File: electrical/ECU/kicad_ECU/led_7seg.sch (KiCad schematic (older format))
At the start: 10 parts

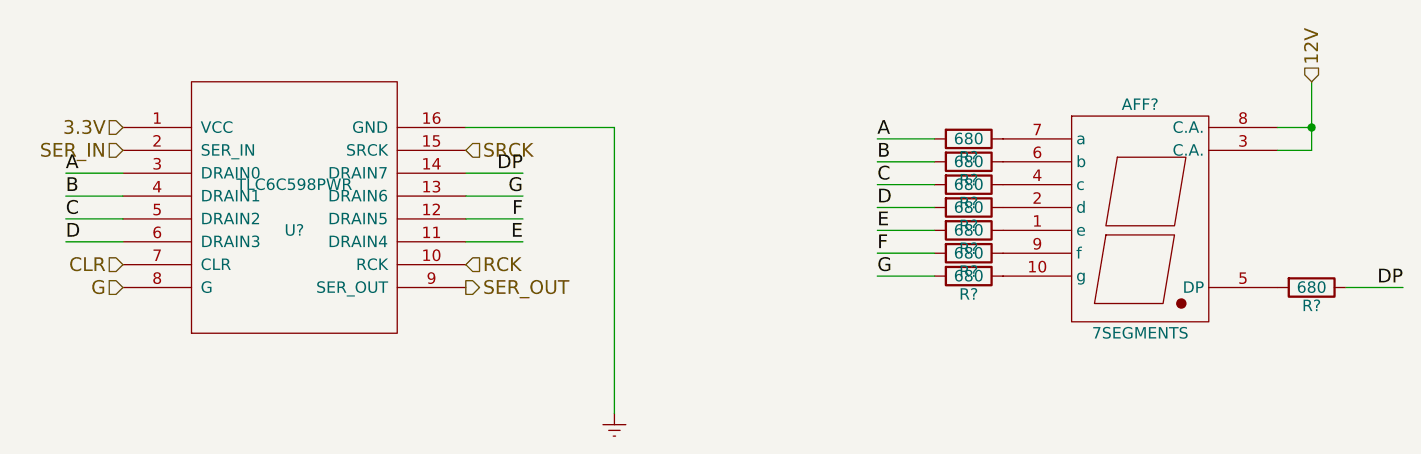
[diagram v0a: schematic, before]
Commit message: fixed some naming errors and initial round of double checking
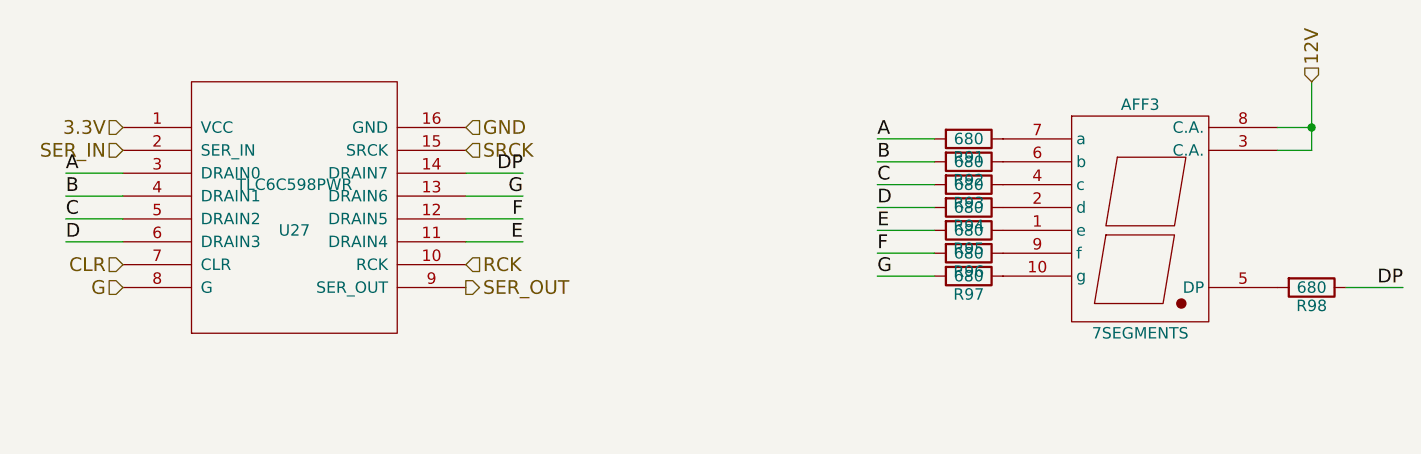
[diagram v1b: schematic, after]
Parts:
- gave numbers to parts that had none: 10
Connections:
- net Earth renamed GND
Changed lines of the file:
@@
 $Descr A4 11693 8268
 encoding utf-8
-Sheet 25 33
+Sheet 29 33
 Title ""
 Date ""
@@
 $EndDescr
 $Comp
-L 7SEGMENTS AFF?
+L 7SEGMENTS AFF1
 U 1 1 597A01F6
 P 7800 3550
-AR Path="/5978A36B/597907E6/597A01ED/597A01F6" Ref="AFF?"  Part="1"
-AR Path="/5978A36B/597907E6/597CC151/597A01F6" Ref="AFF?"  Part="1"
-AR Path="/5978A36B/597907E6/597CC684/597A01F6" Ref="AFF?"  Part="1"
-F 0 "AFF?" H 7800 4100 50  0000 C CNN
+AR Path="/5978A36B/597907E6/597A01ED/597A01F6" Ref="AFF1"  Part="1"
+AR Path="/5978A36B/597907E6/597CC151/597A01F6" Ref="AFF2"  Part="1"
+AR Path="/5978A36B/597907E6/597CC684/597A01F6" Ref="AFF3"  Part="1"
+F 0 "AFF3" H 7800 4100 50  0000 C CNN
 F 1 "7SEGMENTS" H 7800 3100 50  0000 C CNN
 F 2 "" H 7800 3550 50  0001 C CNN
@@
 $EndComp
 $Comp
-L TLC6C598PWR U?
+L TLC6C598PWR U25
 U 1 1 597A021D
 P 4100 3450
-AR Path="/5978A36B/597907E6/597A01ED/597A021D" Ref="U?"  Part="1"
-AR Path="/5978A36B/597907E6/597CC151/597A021D" Ref="U?"  Part="1"
-AR Path="/5978A36B/597907E6/597CC684/597A021D" Ref="U?"  Part="1"
-F 0 "U?" H 4100 3350 50  0000 C CNN
+AR Path="/5978A36B/597907E6/597A01ED/597A021D" Ref="U25"  Part="1"
+AR Path="/5978A36B/597907E6/597CC151/597A021D" Ref="U26"  Part="1"
+AR Path="/5978A36B/597907E6/597CC684/597A021D" Ref="U27"  Part="1"
+F 0 "U27" H 4100 3350 50  0000 C CNN
 F 1 "TLC6C598PWR" H 4100 3550 50  0000 C CNN
 F 2 "MODULE" H 4100 3450 50  0001 C CNN
@@
 SER_OUT
 $Comp
-L R R?
+L R R75
 U 1 1 597A0AE9
 P 7050 3150
-AR Path="/5978A36B/597907E6/597A01ED/597A0AE9" Ref="R?"  Part="1"
-AR Path="/5978A36B/597907E6/597CC151/597A0AE9" Ref="R?"  Part="1"
-AR Path="/5978A36B/597907E6/597CC684/597A0AE9" Ref="R?"  Part="1"
-F 0 "R?" V 7130 3150 50  0000 C CNN
+AR Path="/5978A36B/597907E6/597A01ED/597A0AE9" Ref="R75"  Part="1"
+AR Path="/5978A36B/597907E6/597CC151/597A0AE9" Ref="R83"  Part="1"
+AR Path="/5978A36B/597907E6/597CC684/597A0AE9" Ref="R91"  Part="1"
+F 0 "R91" V 7130 3150 50  0000 C CNN
 F 1 "680" V 7050 3150 50  0000 C CNN
 F 2 "" V 6980 3150 50  0001 C CNN
@@
 $EndComp
 $Comp
-L R R?
+L R R76
 U 1 1 597A0B81
 P 7050 3250
-AR Path="/5978A36B/597907E6/597A01ED/597A0B81" Ref="R?"  Part="1"
-AR Path="/5978A36B/597907E6/597CC151/597A0B81" Ref="R?"  Part="1"
-AR Path="/5978A36B/597907E6/597CC684/597A0B81" Ref="R?"  Part="1"
-F 0 "R?" V 7130 3250 50  0000 C CNN
+AR Path="/5978A36B/597907E6/597A01ED/597A0B81" Ref="R76"  Part="1"
+AR Path="/5978A36B/597907E6/597CC151/597A0B81" Ref="R84"  Part="1"
+AR Path="/5978A36B/597907E6/597CC684/597A0B81" Ref="R92"  Part="1"
+F 0 "R92" V 7130 3250 50  0000 C CNN
 F 1 "680" V 7050 3250 50  0000 C CNN
 F 2 "" V 6980 3250 50  0001 C CNN
@@
 $EndComp
 $Comp
-L R R?
+L R R77
 U 1 1 597A0BBD
 P 7050 3350
-AR Path="/5978A36B/597907E6/597A01ED/597A0BBD" Ref="R?"  Part="1"
-AR Path="/5978A36B/597907E6/597CC151/597A0BBD" Ref="R?"  Part="1"
-AR Path="/5978A36B/597907E6/597CC684/597A0BBD" Ref="R?"  Part="1"
-F 0 "R?" V 7130 3350 50  0000 C CNN
+AR Path="/5978A36B/597907E6/597A01ED/597A0BBD" Ref="R77"  Part="1"
+AR Path="/5978A36B/597907E6/597CC151/597A0BBD" Ref="R85"  Part="1"
+AR Path="/5978A36B/597907E6/597CC684/597A0BBD" Ref="R93"  Part="1"
+F 0 "R93" V 7130 3350 50  0000 C CNN
 F 1 "680" V 7050 3350 50  0000 C CNN
 F 2 "" V 6980 3350 50  0001 C CNN
@@
 $EndComp
 $Comp
-L R R?
+L R R78
 U 1 1 597A0BC3
 P 7050 3450
-AR Path="/5978A36B/597907E6/597A01ED/597A0BC3" Ref="R?"  Part="1"
-AR Path="/5978A36B/597907E6/597CC151/597A0BC3" Ref="R?"  Part="1"
-AR Path="/5978A36B/597907E6/597CC684/597A0BC3" Ref="R?"  Part="1"
-F 0 "R?" V 7130 3450 50  0000 C CNN
+AR Path="/5978A36B/597907E6/597A01ED/597A0BC3" Ref="R78"  Part="1"
+AR Path="/5978A36B/597907E6/597CC151/597A0BC3" Ref="R86"  Part="1"
+AR Path="/5978A36B/597907E6/597CC684/597A0BC3" Ref="R94"  Part="1"
+F 0 "R94" V 7130 3450 50  0000 C CNN
 F 1 "680" V 7050 3450 50  0000 C CNN
 F 2 "" V 6980 3450 50  0001 C CNN
@@
 $EndComp
 $Comp
-L R R?
+L R R79
 U 1 1 597A0C0D
 P 7050 3550
-AR Path="/5978A36B/597907E6/597A01ED/597A0C0D" Ref="R?"  Part="1"
-AR Path="/5978A36B/597907E6/597CC151/597A0C0D" Ref="R?"  Part="1"
-AR Path="/5978A36B/597907E6/597CC684/597A0C0D" Ref="R?"  Part="1"
-F 0 "R?" V 7130 3550 50  0000 C CNN
+AR Path="/5978A36B/597907E6/597A01ED/597A0C0D" Ref="R79"  Part="1"
+AR Path="/5978A36B/597907E6/597CC151/597A0C0D" Ref="R87"  Part="1"
+AR Path="/5978A36B/597907E6/597CC684/597A0C0D" Ref="R95"  Part="1"
+F 0 "R95" V 7130 3550 50  0000 C CNN
 F 1 "680" V 7050 3550 50  0000 C CNN
 F 2 "" V 6980 3550 50  0001 C CNN
@@
 $EndComp
 $Comp
-L R R?
+L R R80
 U 1 1 597A0C13
 P 7050 3650
-AR Path="/5978A36B/597907E6/597A01ED/597A0C13" Ref="R?"  Part="1"
-AR Path="/5978A36B/597907E6/597CC151/597A0C13" Ref="R?"  Part="1"
-AR Path="/5978A36B/597907E6/597CC684/597A0C13" Ref="R?"  Part="1"
-F 0 "R?" V 7130 3650 50  0000 C CNN
+AR Path="/5978A36B/597907E6/597A01ED/597A0C13" Ref="R80"  Part="1"
+AR Path="/5978A36B/597907E6/597CC151/597A0C13" Ref="R88"  Part="1"
+AR Path="/5978A36B/597907E6/597CC684/597A0C13" Ref="R96"  Part="1"
+F 0 "R96" V 7130 3650 50  0000 C CNN
 F 1 "680" V 7050 3650 50  0000 C CNN
 F 2 "" V 6980 3650 50  0001 C CNN
@@
 $EndComp
 $Comp
-L R R?
+L R R81
 U 1 1 597A0C19
 P 7050 3750
-AR Path="/5978A36B/597907E6/597A01ED/597A0C19" Ref="R?"  Part="1"
-AR Path="/5978A36B/597907E6/597CC151/597A0C19" Ref="R?"  Part="1"
-AR Path="/5978A36B/597907E6/597CC684/597A0C19" Ref="R?"  Part="1"
-F 0 "R?" V 7130 3750 50  0000 C CNN
+AR Path="/5978A36B/597907E6/597A01ED/597A0C19" Ref="R81"  Part="1"
+AR Path="/5978A36B/597907E6/597CC151/597A0C19" Ref="R89"  Part="1"
+AR Path="/5978A36B/597907E6/597CC684/597A0C19" Ref="R97"  Part="1"
+F 0 "R97" V 7130 3750 50  0000 C CNN
 F 1 "680" V 7050 3750 50  0000 C CNN
 F 2 "" V 6980 3750 50  0001 C CNN
@@
 $EndComp
 $Comp
-L R R?
+L R R82
 U 1 1 597A0C64
 P 8550 3800
-AR Path="/5978A36B/597907E6/597A01ED/597A0C64" Ref="R?"  Part="1"
-AR Path="/5978A36B/597907E6/597CC151/597A0C64" Ref="R?"  Part="1"
-AR Path="/5978A36B/597907E6/597CC684/597A0C64" Ref="R?"  Part="1"
-F 0 "R?" V 8630 3800 50  0000 C CNN
+AR Path="/5978A36B/597907E6/597A01ED/597A0C64" Ref="R82"  Part="1"
+AR Path="/5978A36B/597907E6/597CC151/597A0C64" Ref="R90"  Part="1"
+AR Path="/5978A36B/597907E6/597CC684/597A0C64" Ref="R98"  Part="1"
+F 0 "R98" V 8630 3800 50  0000 C CNN
 F 1 "680" V 8550 3800 50  0000 C CNN
 F 2 "" V 8480 3800 50  0001 C CNN
@@
 Text Label 5100 3300 2    60   ~ 0
 DP
-$Comp
-L Earth #PWR?
-U 1 1 597A0EF5
-P 5500 4350
-AR Path="/5978A36B/597907E6/597A01ED/597A0EF5" Ref="#PWR?"  Part="1"
-AR Path="/5978A36B/597907E6/597CC151/597A0EF5" Ref="#PWR?"  Part="1"
-AR Path="/5978A36B/597907E6/597CC684/597A0EF5" Ref="#PWR?"  Part="1"
-F 0 "#PWR?" H 5500 4100 50  0001 C CNN
-F 1 "Earth" H 5500 4200 50  0001 C CNN
-F 2 "" H 5500 4350 50  0001 C CNN
-F 3 "" H 5500 4350 50  0001 C CNN
-	1    5500 4350
-	1    0    0    -1
-$EndComp
-Wire Wire Line
-	4850 3100 5500 3100
-Wire Wire Line
-	5500 3100 5500 4350
+Text HLabel 4850 3100 2    60   Input ~ 0
+GND
 $EndSCHEMATC

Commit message: minor naming change
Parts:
- renumbered AFF1 to AFF2701, R75 to R2701, R76 to R2702, R77 to R2703, R78 to R2704, R79 to R2705, R80 to R2706, R81 to R2707, R82 to R2708, U25 to U2701
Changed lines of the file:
@@
 $EndDescr
 $Comp
-L 7SEGMENTS AFF1
+L 7SEGMENTS AFF2701
 U 1 1 597A01F6
 P 7800 3550
-AR Path="/5978A36B/597907E6/597A01ED/597A01F6" Ref="AFF1"  Part="1"
-AR Path="/5978A36B/597907E6/597CC151/597A01F6" Ref="AFF2"  Part="1"
-AR Path="/5978A36B/597907E6/597CC684/597A01F6" Ref="AFF3"  Part="1"
-F 0 "AFF3" H 7800 4100 50  0000 C CNN
+AR Path="/5978A36B/597907E6/597A01ED/597A01F6" Ref="AFF2701"  Part="1"
+AR Path="/5978A36B/597907E6/597CC151/597A01F6" Ref="AFF2801"  Part="1"
+AR Path="/5978A36B/597907E6/597CC684/597A01F6" Ref="AFF2901"  Part="1"
+F 0 "AFF2901" H 7800 4100 50  0000 C CNN
 F 1 "7SEGMENTS" H 7800 3100 50  0000 C CNN
 F 2 "" H 7800 3550 50  0001 C CNN
@@
 $EndComp
 $Comp
-L TLC6C598PWR U25
+L TLC6C598PWR U2701
 U 1 1 597A021D
 P 4100 3450
-AR Path="/5978A36B/597907E6/597A01ED/597A021D" Ref="U25"  Part="1"
-AR Path="/5978A36B/597907E6/597CC151/597A021D" Ref="U26"  Part="1"
-AR Path="/5978A36B/597907E6/597CC684/597A021D" Ref="U27"  Part="1"
-F 0 "U27" H 4100 3350 50  0000 C CNN
+AR Path="/5978A36B/597907E6/597A01ED/597A021D" Ref="U2701"  Part="1"
+AR Path="/5978A36B/597907E6/597CC151/597A021D" Ref="U2801"  Part="1"
+AR Path="/5978A36B/597907E6/597CC684/597A021D" Ref="U2901"  Part="1"
+F 0 "U2901" H 4100 3350 50  0000 C CNN
 F 1 "TLC6C598PWR" H 4100 3550 50  0000 C CNN
 F 2 "MODULE" H 4100 3450 50  0001 C CNN
@@
 SER_OUT
 $Comp
-L R R75
+L R R2701
 U 1 1 597A0AE9
 P 7050 3150
-AR Path="/5978A36B/597907E6/597A01ED/597A0AE9" Ref="R75"  Part="1"
-AR Path="/5978A36B/597907E6/597CC151/597A0AE9" Ref="R83"  Part="1"
-AR Path="/5978A36B/597907E6/597CC684/597A0AE9" Ref="R91"  Part="1"
-F 0 "R91" V 7130 3150 50  0000 C CNN
+AR Path="/5978A36B/597907E6/597A01ED/597A0AE9" Ref="R2701"  Part="1"
+AR Path="/5978A36B/597907E6/597CC151/597A0AE9" Ref="R2801"  Part="1"
+AR Path="/5978A36B/597907E6/597CC684/597A0AE9" Ref="R2901"  Part="1"
+F 0 "R2901" V 7130 3150 50  0000 C CNN
 F 1 "680" V 7050 3150 50  0000 C CNN
 F 2 "" V 6980 3150 50  0001 C CNN
@@
 $EndComp
 $Comp
-L R R76
+L R R2702
 U 1 1 597A0B81
 P 7050 3250
-AR Path="/5978A36B/597907E6/597A01ED/597A0B81" Ref="R76"  Part="1"
-AR Path="/5978A36B/597907E6/597CC151/597A0B81" Ref="R84"  Part="1"
-AR Path="/5978A36B/597907E6/597CC684/597A0B81" Ref="R92"  Part="1"
-F 0 "R92" V 7130 3250 50  0000 C CNN
+AR Path="/5978A36B/597907E6/597A01ED/597A0B81" Ref="R2702"  Part="1"
+AR Path="/5978A36B/597907E6/597CC151/597A0B81" Ref="R2802"  Part="1"
+AR Path="/5978A36B/597907E6/597CC684/597A0B81" Ref="R2902"  Part="1"
+F 0 "R2902" V 7130 3250 50  0000 C CNN
 F 1 "680" V 7050 3250 50  0000 C CNN
 F 2 "" V 6980 3250 50  0001 C CNN
@@
 $EndComp
 $Comp
-L R R77
+L R R2703
 U 1 1 597A0BBD
 P 7050 3350
-AR Path="/5978A36B/597907E6/597A01ED/597A0BBD" Ref="R77"  Part="1"
-AR Path="/5978A36B/597907E6/597CC151/597A0BBD" Ref="R85"  Part="1"
-AR Path="/5978A36B/597907E6/597CC684/597A0BBD" Ref="R93"  Part="1"
-F 0 "R93" V 7130 3350 50  0000 C CNN
+AR Path="/5978A36B/597907E6/597A01ED/597A0BBD" Ref="R2703"  Part="1"
+AR Path="/5978A36B/597907E6/597CC151/597A0BBD" Ref="R2803"  Part="1"
+AR Path="/5978A36B/597907E6/597CC684/597A0BBD" Ref="R2903"  Part="1"
+F 0 "R2903" V 7130 3350 50  0000 C CNN
 F 1 "680" V 7050 3350 50  0000 C CNN
 F 2 "" V 6980 3350 50  0001 C CNN
@@
 $EndComp
 $Comp
-L R R78
+L R R2704
 U 1 1 597A0BC3
 P 7050 3450
-AR Path="/5978A36B/597907E6/597A01ED/597A0BC3" Ref="R78"  Part="1"
-AR Path="/5978A36B/597907E6/597CC151/597A0BC3" Ref="R86"  Part="1"
-AR Path="/5978A36B/597907E6/597CC684/597A0BC3" Ref="R94"  Part="1"
-F 0 "R94" V 7130 3450 50  0000 C CNN
+AR Path="/5978A36B/597907E6/597A01ED/597A0BC3" Ref="R2704"  Part="1"
+AR Path="/5978A36B/597907E6/597CC151/597A0BC3" Ref="R2804"  Part="1"
+AR Path="/5978A36B/597907E6/597CC684/597A0BC3" Ref="R2904"  Part="1"
+F 0 "R2904" V 7130 3450 50  0000 C CNN
 F 1 "680" V 7050 3450 50  0000 C CNN
 F 2 "" V 6980 3450 50  0001 C CNN
@@
 $EndComp
 $Comp
-L R R79
+L R R2705
 U 1 1 597A0C0D
 P 7050 3550
-AR Path="/5978A36B/597907E6/597A01ED/597A0C0D" Ref="R79"  Part="1"
-AR Path="/5978A36B/597907E6/597CC151/597A0C0D" Ref="R87"  Part="1"
-AR Path="/5978A36B/597907E6/597CC684/597A0C0D" Ref="R95"  Part="1"
-F 0 "R95" V 7130 3550 50  0000 C CNN
+AR Path="/5978A36B/597907E6/597A01ED/597A0C0D" Ref="R2705"  Part="1"
+AR Path="/5978A36B/597907E6/597CC151/597A0C0D" Ref="R2805"  Part="1"
+AR Path="/5978A36B/597907E6/597CC684/597A0C0D" Ref="R2905"  Part="1"
+F 0 "R2905" V 7130 3550 50  0000 C CNN
 F 1 "680" V 7050 3550 50  0000 C CNN
 F 2 "" V 6980 3550 50  0001 C CNN
@@
 $EndComp
 $Comp
-L R R80
+L R R2706
 U 1 1 597A0C13
 P 7050 3650
-AR Path="/5978A36B/597907E6/597A01ED/597A0C13" Ref="R80"  Part="1"
-AR Path="/5978A36B/597907E6/597CC151/597A0C13" Ref="R88"  Part="1"
-AR Path="/5978A36B/597907E6/597CC684/597A0C13" Ref="R96"  Part="1"
-F 0 "R96" V 7130 3650 50  0000 C CNN
+AR Path="/5978A36B/597907E6/597A01ED/597A0C13" Ref="R2706"  Part="1"
+AR Path="/5978A36B/597907E6/597CC151/597A0C13" Ref="R2806"  Part="1"
+AR Path="/5978A36B/597907E6/597CC684/597A0C13" Ref="R2906"  Part="1"
+F 0 "R2906" V 7130 3650 50  0000 C CNN
 F 1 "680" V 7050 3650 50  0000 C CNN
 F 2 "" V 6980 3650 50  0001 C CNN
@@
 $EndComp
 $Comp
-L R R81
+L R R2707
 U 1 1 597A0C19
 P 7050 3750
-AR Path="/5978A36B/597907E6/597A01ED/597A0C19" Ref="R81"  Part="1"
-AR Path="/5978A36B/597907E6/597CC151/597A0C19" Ref="R89"  Part="1"
-AR Path="/5978A36B/597907E6/597CC684/597A0C19" Ref="R97"  Part="1"
-F 0 "R97" V 7130 3750 50  0000 C CNN
+AR Path="/5978A36B/597907E6/597A01ED/597A0C19" Ref="R2707"  Part="1"
+AR Path="/5978A36B/597907E6/597CC151/597A0C19" Ref="R2807"  Part="1"
+AR Path="/5978A36B/597907E6/597CC684/597A0C19" Ref="R2907"  Part="1"
+F 0 "R2907" V 7130 3750 50  0000 C CNN
 F 1 "680" V 7050 3750 50  0000 C CNN
 F 2 "" V 6980 3750 50  0001 C CNN
@@
 $EndComp
 $Comp
-L R R82
+L R R2708
 U 1 1 597A0C64
 P 8550 3800
-AR Path="/5978A36B/597907E6/597A01ED/597A0C64" Ref="R82"  Part="1"
-AR Path="/5978A36B/597907E6/597CC151/597A0C64" Ref="R90"  Part="1"
-AR Path="/5978A36B/597907E6/597CC684/597A0C64" Ref="R98"  Part="1"
-F 0 "R98" V 8630 3800 50  0000 C CNN
+AR Path="/5978A36B/597907E6/597A01ED/597A0C64" Ref="R2708"  Part="1"
+AR Path="/5978A36B/597907E6/597CC151/597A0C64" Ref="R2808"  Part="1"
+AR Path="/5978A36B/597907E6/597CC684/597A0C64" Ref="R2908"  Part="1"
+F 0 "R2908" V 8630 3800 50  0000 C CNN
 F 1 "680" V 8550 3800 50  0000 C CNN
 F 2 "" V 8480 3800 50  0001 C CNN
